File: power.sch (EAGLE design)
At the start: 7 parts, among them X1 5566-4-RIGHTANGLE, X3 RASPI_BOARD_B+#_H

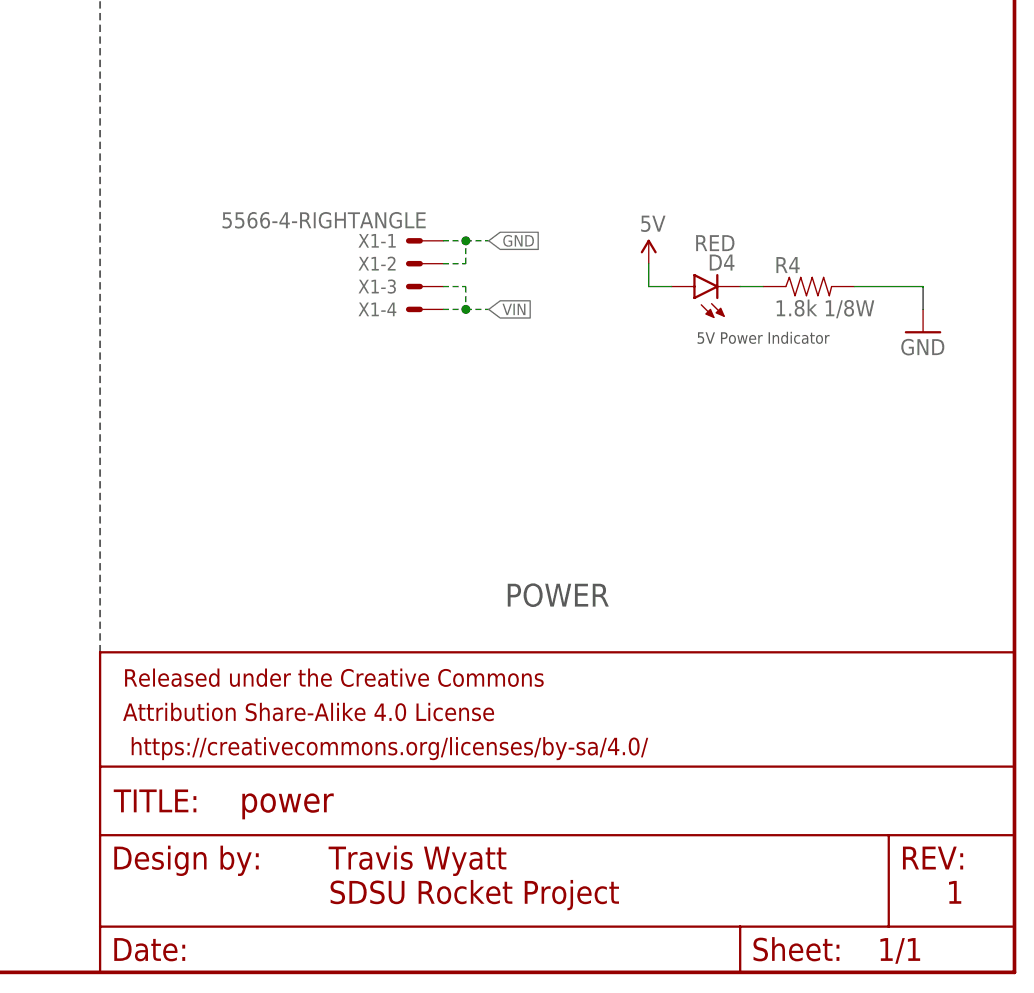
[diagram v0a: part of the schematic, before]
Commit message: Fix molex connector thru hole size
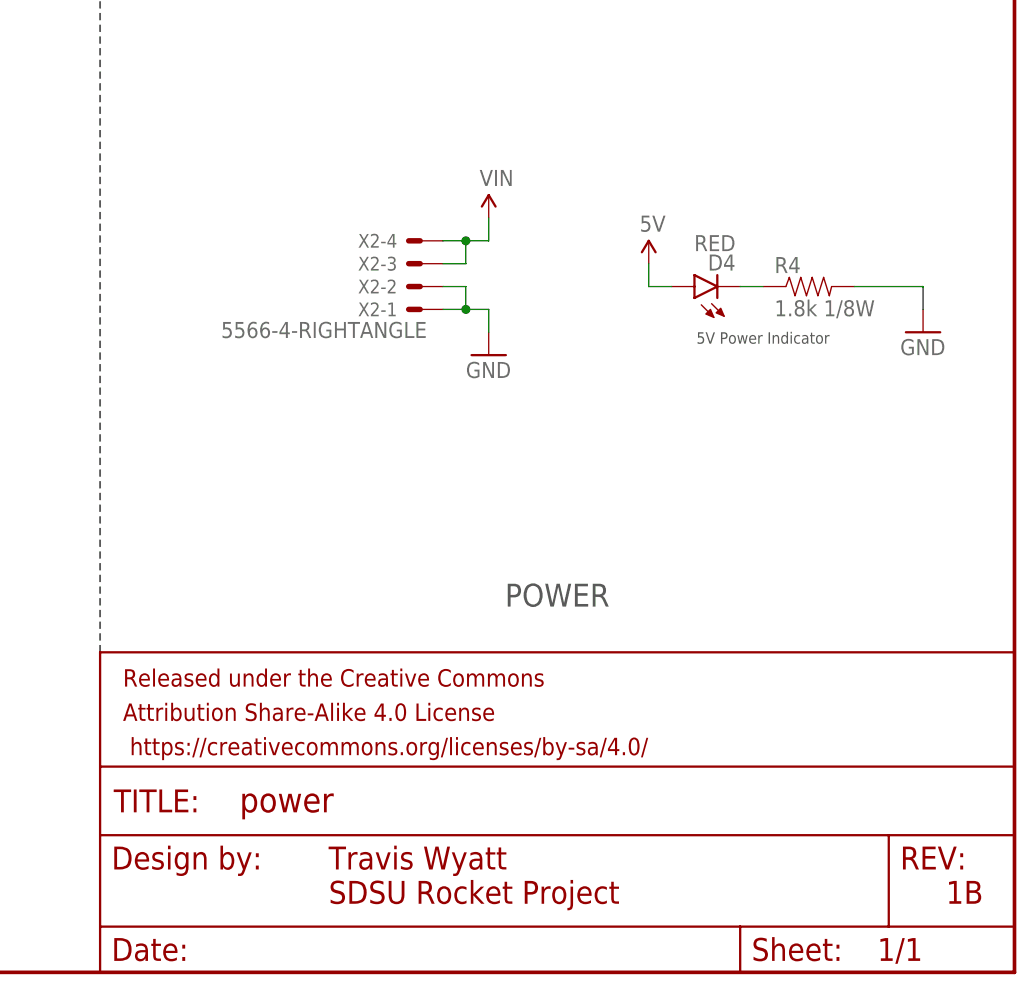
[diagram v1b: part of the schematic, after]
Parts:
- removed X1: 5566-4-RIGHTANGLE, SDSURocket-BreakoutBoards:5566-4-RIGHTANGLE
- added X2: 5566-4-RIGHTANGLE, SDSURocket-Connectors:5566-4-RIGHTANGLE
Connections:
- net GND: now also X2-1.S, X2-2.S; no longer X1-1.S, X1-2.S
- net VIN: now also X2-3.S, X2-4.S; no longer X1-3.S, X1-4.S
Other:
- note added: "1B"
- note removed: "1"
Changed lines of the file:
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@@
 <setting verticaltext="up"/>
 </settings>
-<grid distance="0.1" unitdist="inch" unit="inch" style="lines" multiple="1" display="no" altdistance="0.01" altunitdist="inch" altunit="inch"/>
+<grid distance="0.1" unitdist="inch" unit="inch" style="dots" multiple="1" display="yes" altdistance="0.01" altunitdist="inch" altunit="inch"/>
 <layers>
 <layer number="1" name="Top" color="4" fill="1" visible="no" active="no"/>
@@
 <layer number="56" name="wert" color="7" fill="1" visible="no" active="no"/>
 <layer number="57" name="tCAD" color="7" fill="1" visible="no" active="no"/>
+<layer number="59" name="tCarbon" color="7" fill="1" visible="no" active="no"/>
+<layer number="60" name="bCarbon" color="7" fill="1" visible="no" active="no"/>
 <layer number="90" name="Modules" color="5" fill="1" visible="yes" active="yes"/>
 <layer number="91" name="Nets" color="2" fill="1" visible="yes" active="yes"/>
@@
 <layer number="127" name="_tValues" color="7" fill="1" visible="yes" active="yes"/>
 <layer number="128" name="_bValues" color="7" fill="1" visible="yes" active="yes"/>
+<layer number="129" name="Mask" color="7" fill="1" visible="yes" active="yes"/>
 <layer number="131" name="tAdjust" color="7" fill="1" visible="yes" active="yes"/>
 <layer number="132" name="bAdjust" color="7" fill="1" visible="yes" active="yes"/>
@@
 <layer number="251" name="SMDround" color="12" fill="11" visible="no" active="no"/>
 <layer number="254" name="cooling" color="7" fill="1" visible="yes" active="yes"/>
+<layer number="255" name="routoute" color="7" fill="1" visible="yes" active="yes"/>
 </layers>
 <schematic xreflabel="%F%N/%S.%C%R" xrefpart="/%S.%C%R">
@@
 <part name="R2" library="SparkFun-Resistors" deviceset="RESISTOR" device="0603-RES" value="1.33k 1/10W"/>
 <part name="FRAME1" library="SparkFun-Aesthetics" deviceset="FRAME-LETTER" device=""/>
-<part name="X1" library="SDSURocket-BreakoutBoards" deviceset="5566-4" device="-RIGHTANGLE"/>
 <part name="D4" library="SparkFun-LED" deviceset="LED" device="0603" value="RED"/>
 <part name="R4" library="SparkFun-Resistors" deviceset="RESISTOR" device="0603-RES" value="1.8k 1/8W"/>
 <part name="GND1" library="SparkFun-Aesthetics" deviceset="GND" device=""/>
 <part name="SUPPLY2" library="SparkFun-Aesthetics" deviceset="5V" device=""/>
+<part name="X2" library="SDSURocket-Connectors" deviceset="5566-4" device="-RIGHTANGLE"/>
+<part name="SUPPLY5" library="SparkFun-Aesthetics" deviceset="VIN" device=""/>
+<part name="GND5" library="SparkFun-Aesthetics" deviceset="GND" device=""/>
 </parts>
 <sheets>
@@
 <text x="220.98" y="71.12" size="1.27" layer="97" align="top-center">5V Power Indicator</text>
 <text x="198.12" y="40.64" size="2.54" layer="97" align="bottom-center">POWER</text>
-<text x="241.3" y="7.62" size="2.54" layer="94">1</text>
+<text x="241.3" y="7.62" size="2.54" layer="94">1B</text>
 <text x="172.72" y="12.7" size="2.54" layer="94" align="center-left">Travis Wyatt</text>
 <text x="172.72" y="8.89" size="2.54" layer="94" align="center-left">SDSU Rocket Project</text>
@@
 <instance part="FRAME1" gate="G$1" x="0" y="0"/>
 <instance part="FRAME1" gate="V" x="147.32" y="0"/>
-<instance part="X1" gate="-1" x="182.88" y="81.28" rot="MR0"/>
-<instance part="X1" gate="-2" x="182.88" y="78.74" rot="MR0"/>
-<instance part="X1" gate="-3" x="182.88" y="76.2" rot="MR0"/>
-<instance part="X1" gate="-4" x="182.88" y="73.66" rot="MR0"/>
 <instance part="D4" gate="G$1" x="213.36" y="76.2" rot="R90"/>
 <instance part="R4" gate="G$1" x="226.06" y="76.2"/>
 <instance part="GND1" gate="1" x="238.76" y="71.12"/>
 <instance part="SUPPLY2" gate="G$1" x="208.28" y="78.74"/>
+<instance part="X2" gate="-1" x="182.88" y="73.66" rot="R180"/>
+<instance part="X2" gate="-2" x="182.88" y="76.2" rot="R180"/>
+<instance part="X2" gate="-3" x="182.88" y="78.74" rot="R180"/>
+<instance part="X2" gate="-4" x="182.88" y="81.28" rot="R180"/>
+<instance part="SUPPLY5" gate="G$1" x="190.5" y="83.82"/>
+<instance part="GND5" gate="1" x="190.5" y="68.58"/>
 </instances>
 <busses>
@@
 </segment>
 <segment>
-<pinref part="X1" gate="-1" pin="S"/>
-<wire x1="185.42" y1="81.28" x2="187.96" y2="81.28" width="0.1524" layer="91" style="longdash"/>
-<pinref part="X1" gate="-2" pin="S"/>
-<wire x1="187.96" y1="81.28" x2="190.5" y2="81.28" width="0.1524" layer="91" style="longdash"/>
-<wire x1="185.42" y1="78.74" x2="187.96" y2="78.74" width="0.1524" layer="91" style="longdash"/>
-<wire x1="187.96" y1="78.74" x2="187.96" y2="81.28" width="0.1524" layer="91" style="longdash"/>
-<junction x="187.96" y="81.28"/>
-<label x="190.5" y="81.28" size="1.27" layer="95" xref="yes"/>
+<pinref part="X2" gate="-1" pin="S"/>
+<pinref part="GND5" gate="1" pin="GND"/>
+<wire x1="185.42" y1="73.66" x2="187.96" y2="73.66" width="0.1524" layer="91"/>
+<wire x1="187.96" y1="73.66" x2="190.5" y2="73.66" width="0.1524" layer="91"/>
+<wire x1="190.5" y1="73.66" x2="190.5" y2="71.12" width="0.1524" layer="91"/>
+<pinref part="X2" gate="-2" pin="S"/>
+<wire x1="185.42" y1="76.2" x2="187.96" y2="76.2" width="0.1524" layer="91"/>
+<wire x1="187.96" y1="76.2" x2="187.96" y2="73.66" width="0.1524" layer="91"/>
+<junction x="187.96" y="73.66"/>
 </segment>
 </net>
@@
 </segment>
 <segment>
-<pinref part="X1" gate="-4" pin="S"/>
-<wire x1="185.42" y1="73.66" x2="187.96" y2="73.66" width="0.1524" layer="91" style="longdash"/>
-<pinref part="X1" gate="-3" pin="S"/>
-<wire x1="187.96" y1="73.66" x2="190.5" y2="73.66" width="0.1524" layer="91" style="longdash"/>
-<wire x1="185.42" y1="76.2" x2="187.96" y2="76.2" width="0.1524" layer="91" style="longdash"/>
-<wire x1="187.96" y1="76.2" x2="187.96" y2="73.66" width="0.1524" layer="91" style="longdash"/>
-<junction x="187.96" y="73.66"/>
-<label x="190.5" y="73.66" size="1.27" layer="95" xref="yes"/>
+<pinref part="X2" gate="-4" pin="S"/>
+<pinref part="SUPPLY5" gate="G$1" pin="VIN"/>
+<wire x1="185.42" y1="81.28" x2="187.96" y2="81.28" width="0.1524" layer="91"/>
+<wire x1="187.96" y1="81.28" x2="190.5" y2="81.28" width="0.1524" layer="91"/>
+<wire x1="190.5" y1="81.28" x2="190.5" y2="83.82" width="0.1524" layer="91"/>
+<pinref part="X2" gate="-3" pin="S"/>
+<wire x1="185.42" y1="78.74" x2="187.96" y2="78.74" width="0.1524" layer="91"/>
+<wire x1="187.96" y1="78.74" x2="187.96" y2="81.28" width="0.1524" layer="91"/>
+<junction x="187.96" y="81.28"/>
 </segment>
 </net>

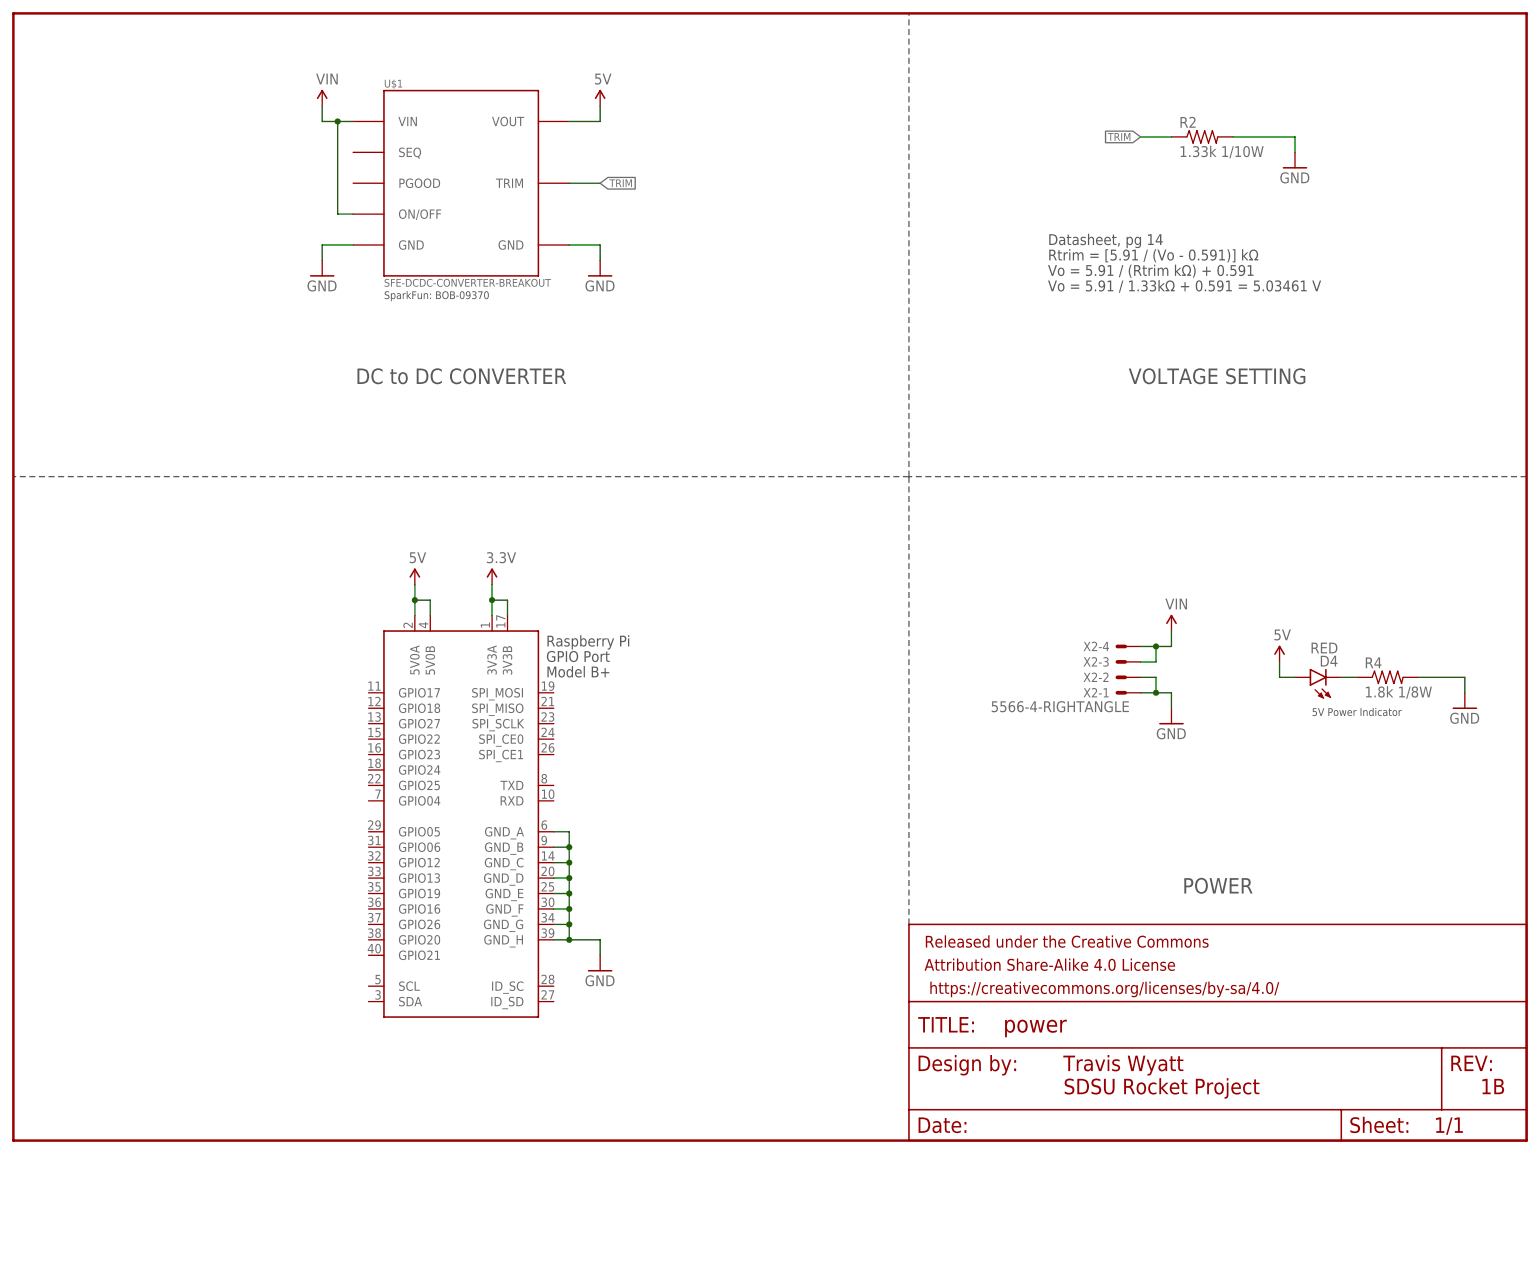
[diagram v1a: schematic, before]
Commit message: Add DC to DC converter and ideal safety diode
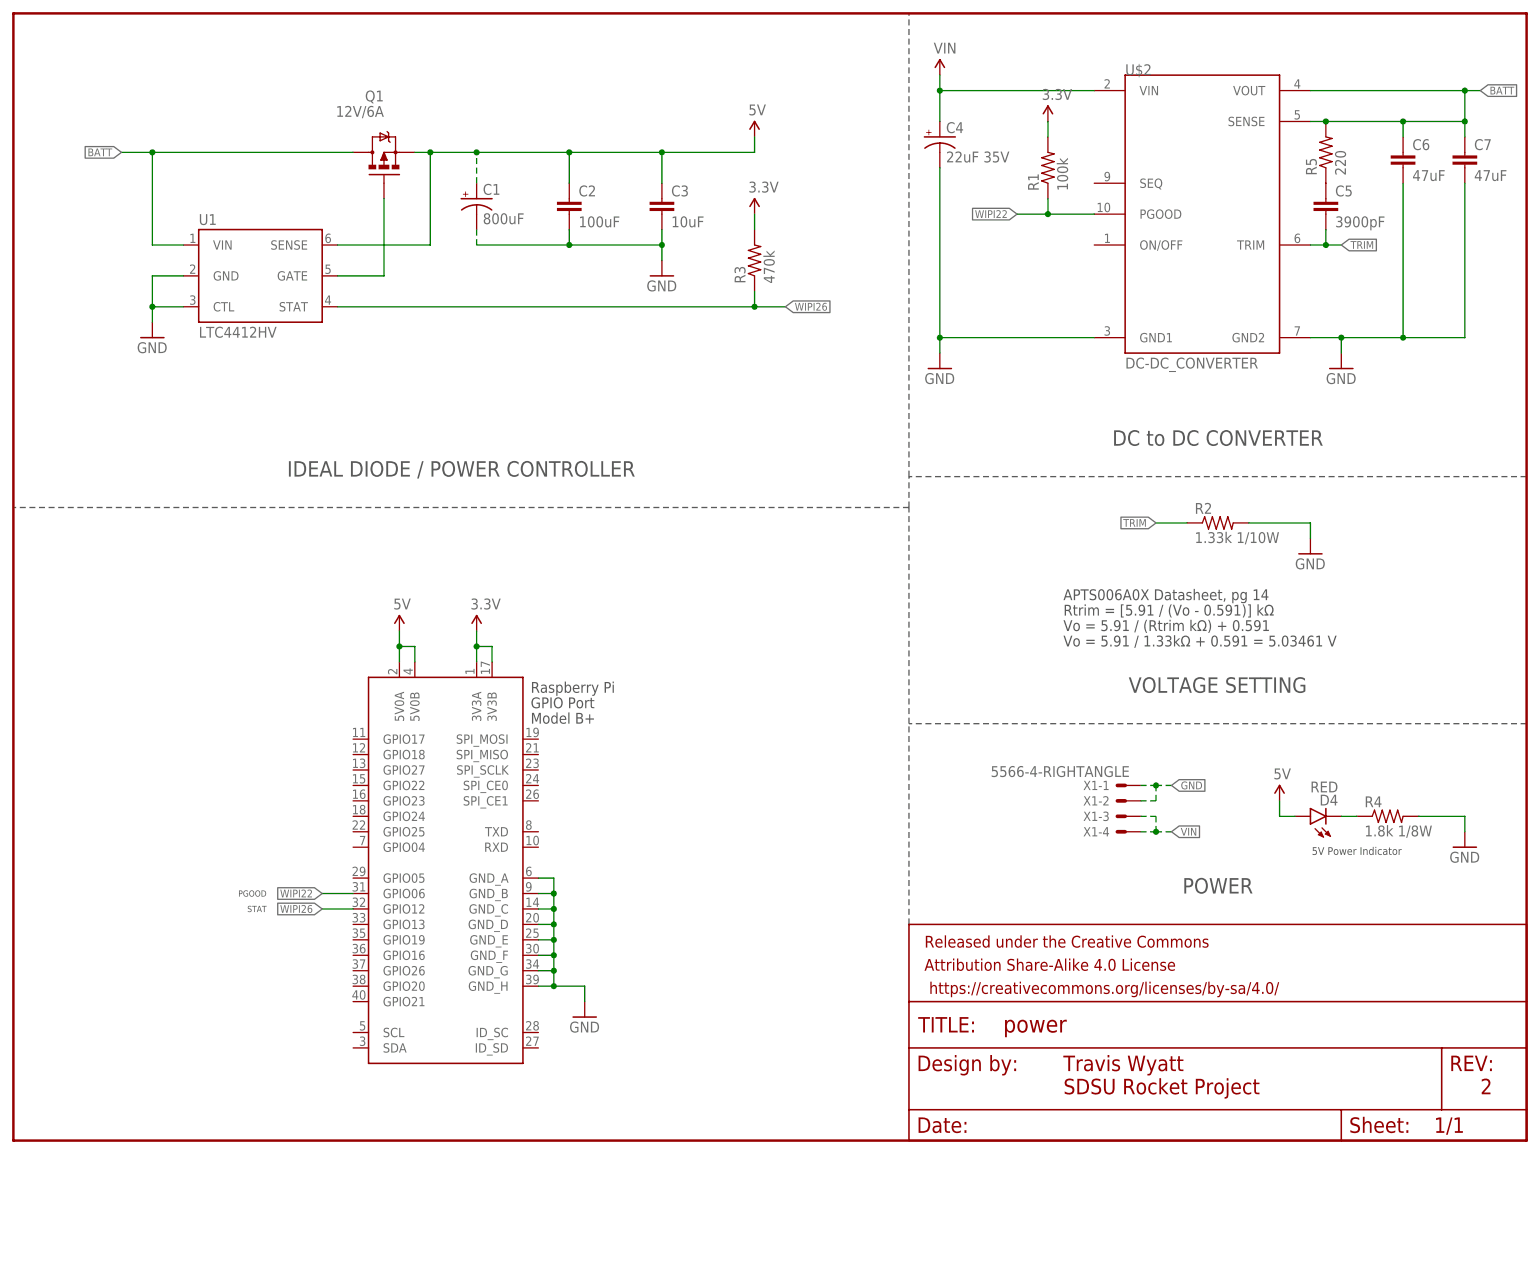
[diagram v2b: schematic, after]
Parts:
- removed U$1: SFE-DCDC-CONVERTER-BREAKOUT, RocketProject:SFE-DCDC-CONVERTER-BREAKOUT
- removed X2: 5566-4-RIGHTANGLE, SDSURocket-Connectors:5566-4-RIGHTANGLE
- added C1: 800uF, SparkFun-Capacitors:CAP_POLG
- added C2: 100uF, SparkFun-Capacitors:CAP0603-CAP
- added C3: 10uF, SparkFun-Capacitors:CAP0603-CAP
- added C4: 22uF 35V, SparkFun-Capacitors:CAP_POLC
- added C5: 3900pF, SparkFun-Capacitors:CAP0603-CAP
- added C6, C7: 47uF, SparkFun-Capacitors:CAP0603-CAP
- added Q1: 12V/6A, SDSURocket-PowerIC:MOSFET-PCHANNEL-FDC606P
- added R1: 100k, SparkFun-Resistors:RESISTOR0603-RES
- added R3: 470k, SparkFun-Passives:RESISTOR0603-RES
- added R5: 220, SparkFun-Passives:RESISTOR0603-RES
- added U$2: DC-DC_CONVERTER, SparkFun-PowerIC:DC-DC_CONVERTER
- added U1: LTC4412HV, SDSURocket-PowerIC:LTC4412HV-SOT-23
- added X1: 5566-4-RIGHTANGLE, SDSURocket-BreakoutBoards:5566-4-RIGHTANGLE
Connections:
- new net BATT: C6.1, C7.1, Q1.D, R5.2, U$2.SENSE, U$2.VOUT, U1.VIN
- new net N$1: Q1.G, U1.GATE
- new net N$2: C5.1, R5.1
- new net WIPI22: R1.1, U$2.PGOOD, X3.GPIO06
- new net WIPI26: R3.1, U1.STAT, X3.GPIO12
- net 3.3V: now also R1.2, R3.2
- net 5V: now also C1.+, C2.1, C3.1, Q1.S, U1.SENSE; no longer U$1.VOUT
- net GND: now also C1.-, C2.2, C3.2, C4.-, C6.2, C7.2, U$2.GND1, U$2.GND2, U1.CTL, U1.GND, X1-1.S, X1-2.S; no longer U$1.GND@1, U$1.GND@2, X2-1.S, X2-2.S
- net TRIM: now also C5.2, U$2.TRIM; no longer U$1.TRIM
- net VIN: now also C4.+, U$2.VIN, X1-3.S, X1-4.S; no longer U$1.ON/OFF, U$1.VIN, X2-3.S, X2-4.S
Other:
- note added: "2"
- note added: "APTS006A0X Datasheet, pg 14"
- note added: "IDEAL DIODE / POWER CONTROLLER"
- note added: "PGOOD"
- note added: "STAT"
- note removed: "1B"
- note removed: "Datasheet, pg 14"
- note removed: "SparkFun: BOB-09370"
- moved on the sheet: D4, R2, R4
